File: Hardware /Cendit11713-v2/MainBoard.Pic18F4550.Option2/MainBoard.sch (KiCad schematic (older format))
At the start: 54 parts, among them CON1 POWER_CON, CON2 ICSP_CON, CON3 USB_CON, J1 RESET_CON, J2 PIN_HEADER_20P, J3 PIN_HEADER_20P, P1 SATA_PLUG _22P_SMT, P2 SATA_PLUG _22P_SMT, U1 PIC18F4550-I/P, U2 MPL3115A2, U3 PCF85263A, Y1 Crystal, Y2 32.768KHZ

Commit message: En CenditLab.Reducido + Cendit11713
  - Hardware tarjeta madre opcion 2, esquematico + PCB
  - Software UI vistas de setup + steps
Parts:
- removed P1, P2: SATA_PLUG _22P_SMT, CenditFootprints:SATA_BACKPLANE_RECEPTACLE_VERTICAL_22P, symbol CONN_01X22
- added D6, D7: LED, LEDs:LED_0805, symbol LED
- added J4, J5: SATA_PLUG _22P_SMT, CenditFootprints:SATA_PLUG_22P_SMT, symbol CONN_01X21
- added LS1: Speaker_Crystal, Buzzers_Beepers:MagneticBuzzer_Kingstate_KCG0601, symbol Speaker_Crystal
- added Q1: 2N2222, TO_SOT_Packages_SMD:TSOT-23, symbol Q_NPN_BCE
- added R12, R13, R14: 300, Resistors_SMD:R_0805_HandSoldering, symbol R_Small
- added R15: 1k, Resistors_SMD:R_0805_HandSoldering, symbol R_Small
- C6, C7: footprint Capacitors_SMD:C_0603_HandSoldering -> Capacitors_SMD:C_0805_HandSoldering
- D1, D2: value D_Schottky -> SP1003-01ETG
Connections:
- net labels added: AGND, GND_PWR, VCC_3V
- net labels removed: VCC
- wire segments 257 -> 269

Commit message: En Cendit11713 diseño de MainBoard Option 2
  - Edicion esquematico +diseño PCB + diseño de fuente
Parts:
- removed CON1: POWER_CON, Pin_Headers:Pin_Header_Straight_2x03_Pitch2.54mm, symbol POWER_CON
- added CON1: POWER_BUS, Pin_Headers:Pin_Header_Straight_2x05, symbol POWER_BUS
- CON2: footprint Pin_Headers:Pin_Header_Straight_2x03_Pitch2.54mm -> Pin_Headers:Pin_Header_Straight_2x03
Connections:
- net labels removed: AGND, VDD_MAIN
- wire segments 269 -> 274
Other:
- moved on the sheet: BT1, C10, C11, C12, C13, C14, C15, C16, C17, C18, C5, C6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

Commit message: En CenditLab + Cendit11713
  - Software trabajo en clases UI + fxml
  - Hardware diseño de tarjeta madre opcion 2
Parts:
- removed J2, J3: PIN_HEADER_20P, Pin_Headers:Pin_Header_Straight_1x20_Pitch2.54mm, symbol CONN_01X20
- removed J5: SATA_PLUG _22P_SMT, CenditFootprints:SATA_PLUG_22P_SMT, symbol CONN_01X21
- removed JP2: JMP5V, Pin_Headers:Pin_Header_Straight_1x02_Pitch2.54mm, symbol Jumper_NC_Small
- removed JP3: JMP3V, Pin_Headers:Pin_Header_Straight_1x02_Pitch2.54mm, symbol Jumper_NO_Small
- added J2: SATA_PLUG _22P_SMT, CenditFootprints2:SATA_PLUG_22P_SMT, symbol CONN_01X21
- added JP2: JMP_3V_5V, Pin_Headers:Pin_Header_Straight_1x03, symbol Jumper_NC_Dual
- added P1, P2: DEBUG_HEADER_21P, CenditFootprints2:DEBUG_PIN_HEADER_21P, symbol CONN_01X21
- added R16, R17, R18, R19, R20, R21, R22, R23, R24, R25, R26, R27, R28, R29, R30, R31, R32, R33, R34, R35, R36, R37, R38, R39, R40, R41, R42, R43, R44, R45: RP, Resistors_SMD:R_0603_HandSoldering, symbol R_Small
- added R46: 0, Resistors_SMD:R_0805_HandSoldering, symbol R_Small
- CON3: footprint CenditFootprints:USB_SMT_B -> CenditFootprints2:USB_SMT_B
- D1, D2, D3, D4, D5: footprint CenditFootprints:SP1003-01ETG -> CenditFootprints2:SP1003-01ETG
- J4: footprint CenditFootprints:SATA_PLUG_22P_SMT -> CenditFootprints2:SATA_PLUG_22P_SMT
- R8: value 1.5K -> 100
- U1: footprint PIC18F4550-I_P:DIP254P1524X635-40 -> CenditFootprints2:PIC18F4550-PDIP
- U2: footprint CenditFootprints:MPL3115A2 -> CenditFootprints2:MPL3115A2
- U3: footprint CenditFootprints:PCF85263A_SO8 -> CenditFootprints2:PCF85263A_SO8
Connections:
- net labels added: D+, D-, RA0, RA1, RA2, RA3, RA4, RA5, RB0, RB1, RB2, RB3, RB4, RB5, RB6, RB7, RC0, RC1, RC2, RC6, RC7, RD0, RD1, RD2, RD3, RD4, RD5, RD6, RD7, RE0, RE1, RE2
- net labels removed: GND
- wire segments 274 -> 308
- no-connect marks 0 -> 2
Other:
- moved on the sheet: BT1, C1, C10, C11, C12, C13, C14, C15, C16, C17, C18, C2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

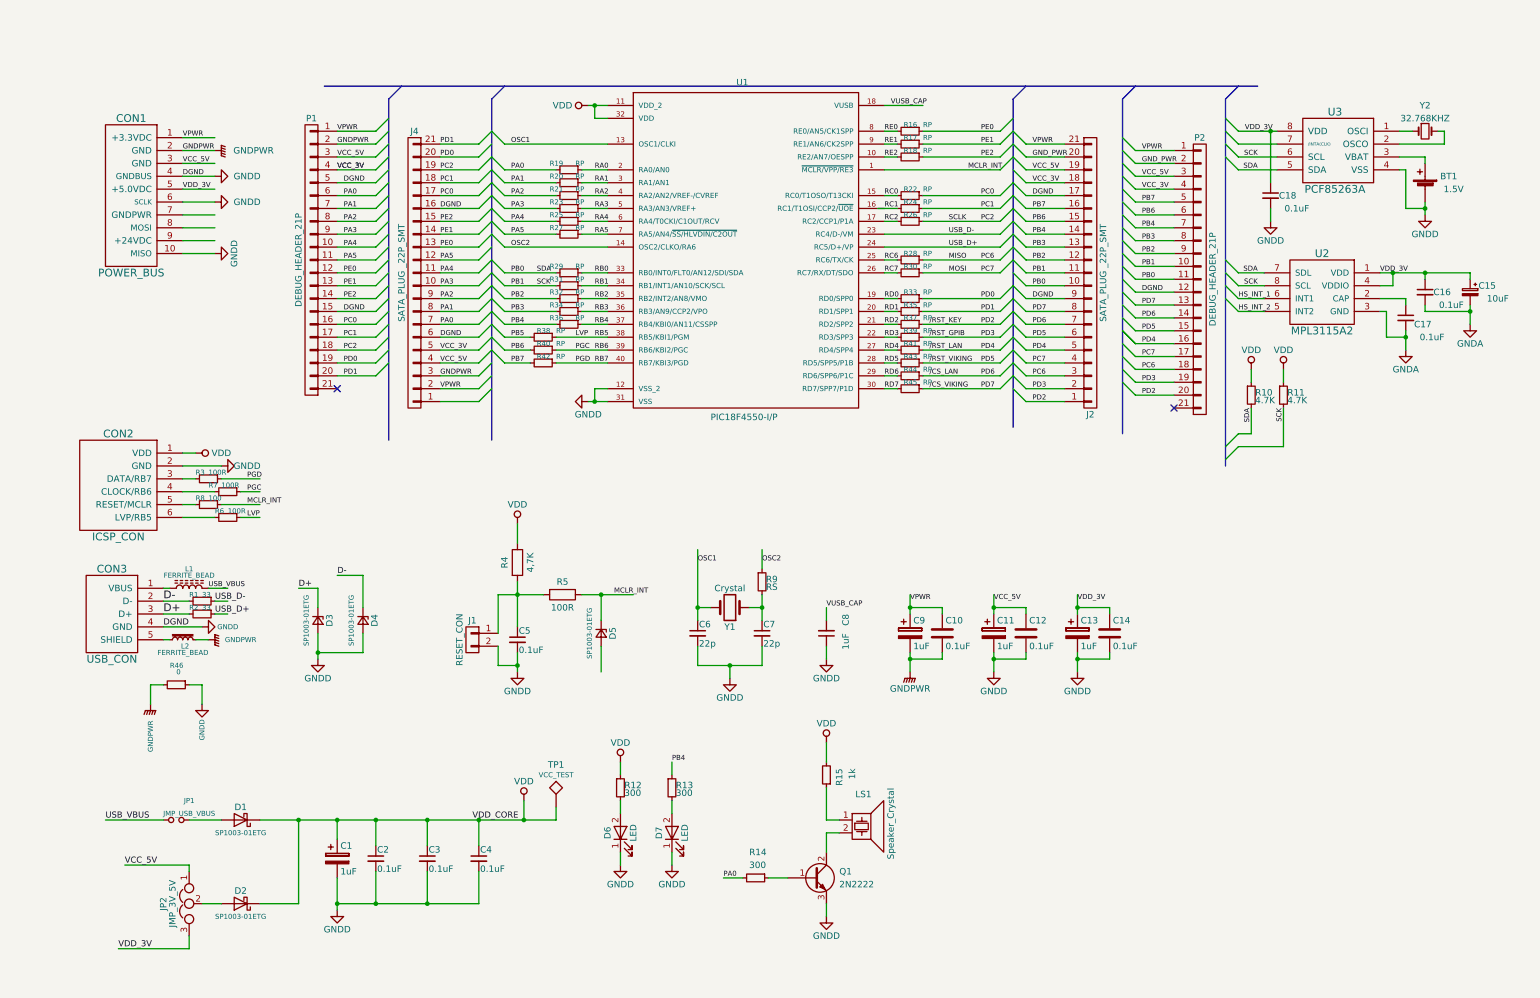
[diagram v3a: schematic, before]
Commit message: En CenditLab + Cendit11713
   - Diseño de clases UI para Steps (TaskExecutionStep)
   - Layout PCB tarjeta madre opcion 2
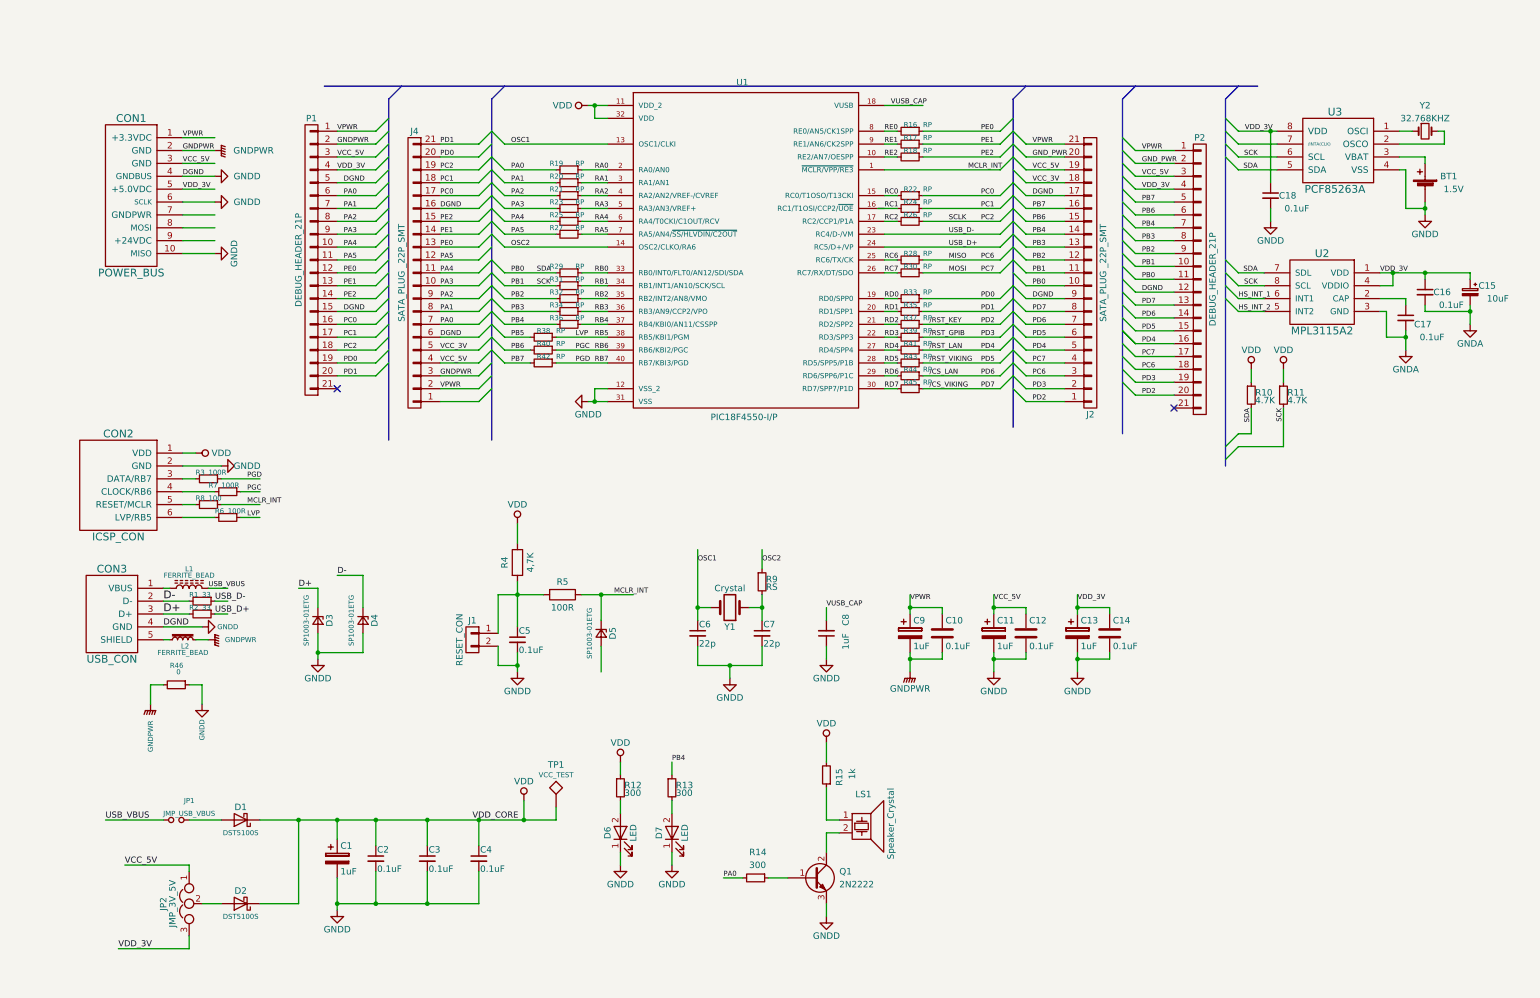
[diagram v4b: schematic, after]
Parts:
- D1, D2: value SP1003-01ETG -> DST5100S; footprint CenditFootprints2:SP1003-01ETG -> CenditFootprints:DST5100S-TO-277B
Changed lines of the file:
@@
 LIBS:74xx
 LIBS:cmos4000
+LIBS:PIC18F4550-I_P
 LIBS:CenditBasic
 LIBS:MainBoard-cache
@@
 P 1950 6600
 F 0 "D1" H 1950 6500 50  0000 C CNN
-F 1 "SP1003-01ETG" H 1950 6700 39  0000 C CNN
-F 2 "CenditFootprints2:SP1003-01ETG" H 1950 6600 50  0001 C CNN
+F 1 "DST5100S" H 1950 6700 39  0000 C CNN
+F 2 "CenditFootprints:DST5100S-TO-277B" H 1950 6600 50  0001 C CNN
 F 3 "" H 1950 6600 50  0001 C CNN
 	1    1950 6600
@@
 P 1950 7250
 F 0 "D2" H 1950 7150 50  0000 C CNN
-F 1 "SP1003-01ETG" H 1950 7350 39  0000 C CNN
-F 2 "CenditFootprints2:SP1003-01ETG" H 1950 7250 50  0001 C CNN
+F 1 "DST5100S" H 1950 7350 39  0000 C CNN
+F 2 "CenditFootprints:DST5100S-TO-277B" H 1950 7250 50  0001 C CNN
 F 3 "" H 1950 7250 50  0001 C CNN
 	1    1950 7250
@@
 VCC_5V
 Text Label 2700 1550 0    39   ~ 0
-VCC_3V
+VDD_3V
 Text Label 2750 1650 0    39   ~ 0
 DGND
-Text Label 2700 1550 0    39   ~ 0
-VCC_3V
 Text Label 8950 1400 0    39   ~ 0
 VPWR
@@
 VCC_5V
 Text Label 8950 1700 0    39   ~ 0
-VCC_3V
+VDD_3V
 Wire Wire Line
 	1050 6950 1550 6950

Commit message: Respaldo rapido
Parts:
- removed C15: 10uF, Capacitors_SMD:C_1206_HandSoldering, symbol CP_Small
- removed C16, C17: 0.1uF, Capacitors_SMD:C_0805_HandSoldering, symbol C_Small
- removed U2: MPL3115A2, CenditFootprints2:MPL3115A2, symbol MPL3115A2
- CON1: footprint Pin_Headers:Pin_Header_Straight_2x05 -> (none)
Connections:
- net labels removed: GNDA, HS_INT_1, HS_INT_2
- wire segments 308 -> 292
- no-connect marks 2 -> 0
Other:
- moved on the sheet: R46

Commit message: En CenditLab + Cendit11713: commit masivo
 - Trabajo en clases + fxml UI
 - Trabajo en main board option 2 + correccion tarjeta expansor Viking
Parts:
- removed C3: 0.1uF, Capacitors_SMD:C_0805_HandSoldering, symbol C_Small
- added C3: 1uF, Capacitors_SMD:C_1206_HandSoldering, symbol CP
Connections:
- net labels removed: VCC_3V
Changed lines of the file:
@@
 LIBS:74xx
 LIBS:cmos4000
-LIBS:PIC18F4550-I_P
 LIBS:CenditBasic
 LIBS:MainBoard-cache
@@
 $EndComp
 $Comp
-L C_Small C3
-U 1 1 59971B35
-P 3400 6900
-F 0 "C3" H 3410 6970 50  0000 L CNN
-F 1 "0.1uF" H 3410 6820 50  0000 L CNN
-F 2 "Capacitors_SMD:C_0805_HandSoldering" H 3400 6900 50  0001 C CNN
-F 3 "" H 3400 6900 50  0001 C CNN
-	1    3400 6900
-	1    0    0    -1
-$EndComp
-$Comp
 L C_Small C4
 U 1 1 59971BE5
@@
 Entry Wire Line
 	7950 1550 8050 1650
-Entry Wire Line
-	7950 1650 8050 1750
 Entry Wire Line
 	7950 1750 8050 1850
@@
 Wire Wire Line
 	3800 6600 3800 6800
-Wire Wire Line
-	3400 6800 3400 6600
 Connection ~ 3400 6600
 Wire Wire Line
@@
 	3000 7000 3000 7250
 Connection ~ 3000 7250
-Wire Wire Line
-	3400 7000 3400 7250
 Connection ~ 3400 7250
 Connection ~ 3800 6600
@@
 Wire Wire Line
 	8350 1650 8050 1650
-Wire Wire Line
-	8050 1750 8350 1750
 Wire Wire Line
 	8350 1850 8050 1850
@@
 VCC_5V
 Text Label 8100 1750 0    39   ~ 0
-VCC_3V
+VDD_3V
 Text Label 8100 1650 0    39   ~ 0
 DGND
@@
 VPWR
 Text Label 3500 3250 0    39   ~ 0
-GNDPWR
+GND_PWR
 Text Label 1500 1900 0    39   ~ 0
-GNDPWR
+GND_PWR
 Text Label 2700 3250 0    39   ~ 0
 VPWR
 Text Label 2700 3150 0    39   ~ 0
-GNDPWR
+GND_PWR
 Text Label 2700 3050 0    39   ~ 0
 VCC_5V
@@
 	0    -1   -1   0
 $EndComp
+$Comp
+L CP C3
+U 1 1 5A1099C4
+P 3400 6900
+F 0 "C3" H 3425 7000 50  0000 L CNN
+F 1 "1uF" H 3425 6800 50  0000 L CNN
+F 2 "Capacitors_SMD:C_1206_HandSoldering" H 3438 6750 50  0001 C CNN
+F 3 "" H 3400 6900 50  0000 C CNN
+	1    3400 6900
+	1    0    0    -1
+$EndComp
+Wire Wire Line
+	3400 6750 3400 6600
+Wire Wire Line
+	3400 7050 3400 7250
+Entry Wire Line
+	7950 1650 8050 1750
+Wire Wire Line
+	8350 1750 8050 1750
 $EndSCHEMATC
